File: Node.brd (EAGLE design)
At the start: 38.1 x 38.1 mm, 70 parts, among them J1 AVR_SPI_PRG_6NS, J2 M04X2, Q1 PMR280UN, Q2 PMR280UN, Q3 PMR280UN, U1 ATMEGA32U4, U2 BLUETOOTH-RN41", U4 L3GD20, U9 RCLAMP0502A, X1 USBSMD

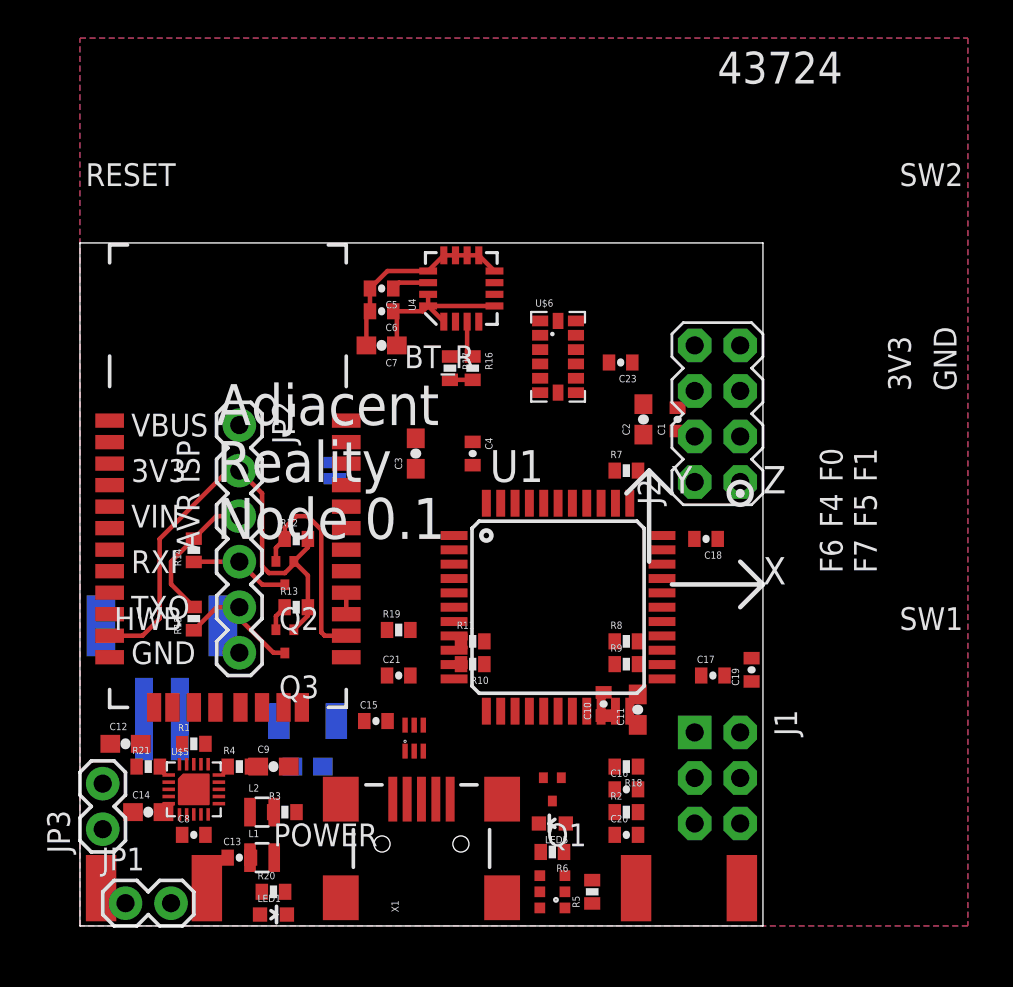
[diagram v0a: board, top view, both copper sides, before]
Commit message: mostly realistic parts placement
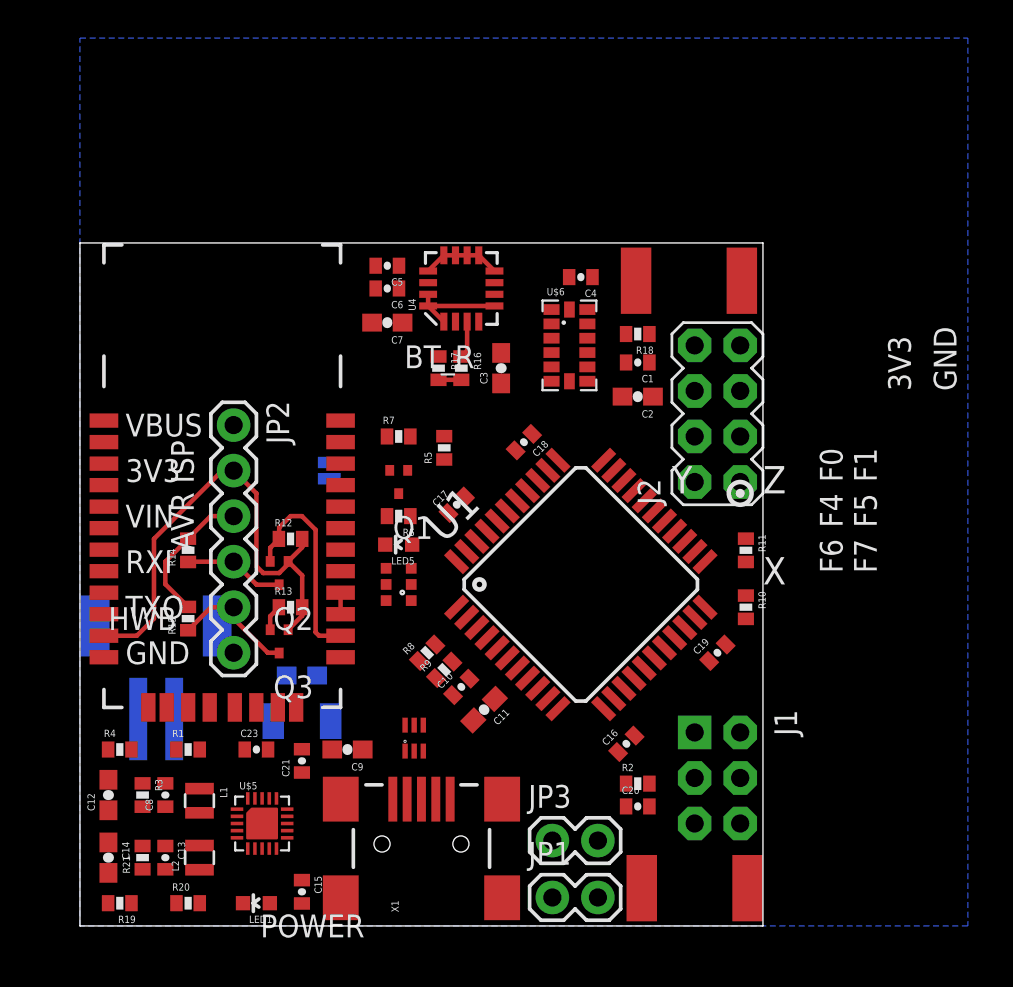
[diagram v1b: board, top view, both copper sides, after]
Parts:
- moved HWB 33.9 mm to (34.0, 36.0), turned to 180 degrees
- moved POWER 30.2 mm to (34.3, 2.11)
- moved C23 29.6 mm to (9.84, 9.84), turned to 0 degrees
- moved R5 26.1 mm to (20.3, 26.7)
- moved JP3 25.1 mm to (26.4, 4.76), turned to 0 degrees
- moved R18 24.1 mm to (31.1, 33.0)
- moved JP1 23.8 mm to (26.4, 1.59)
- moved R19 21.8 mm to (2.22, 1.27), turned to 180 degrees
- moved R6 20.6 mm to (17.8, 22.9)
- moved LED4 19.2 mm to (17.8, 19.1)
- moved Q1 19.2 mm to (17.8, 24.8)
- moved LED5 17.8 mm to (17.8, 21.3)
- moved C17 17.2 mm to (21.0, 23.5), turned to 45 degrees
- moved R11 16.1 mm to (37.1, 21.0), turned to 270 degrees
- moved R10 15.6 mm to (37.1, 17.8), turned to 270 degrees
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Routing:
- net GND: track 11.3 -> 4.42 mm
- net +3V3: track 38.8 -> 34.7 mm
- net N$7: track 2.08 -> 0.00 mm
- removed copper zone on layer 1, net GND
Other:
- board text removed: "43724"
- board text removed: "Adjacent"
- board text removed: "Node 0.1"
- board text removed: "RESET"
- board text removed: "Reality"
- board text removed: "SW1"
- board text removed: "SW2"

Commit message: pass ERC
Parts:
- BAT: value (none) -> JST
- JP1: value (none) -> POWER
- JP2: value (none) -> UART
- JP3: value (none) -> 3V3
- LED1: value (none) -> RED
- LED5: value (none) -> IR
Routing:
- net +3V3: track 34.7 -> 38.7 mm
- net SCL: track 0.00 -> 2.34 mm
- net N$7: track 0.00 -> 2.02 mm

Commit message: mostly pass DRC
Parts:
- moved C6 0.32 mm to (17.1, 35.2)
- moved C7 0.32 mm to (17.1, 33.3)
- moved U4 0.32 mm to (21.3, 35.2)
- moved C3 0.32 mm to (23.5, 30.8)
- moved R16 0.32 mm to (21.3, 30.8)
- moved R17 0.32 mm to (20.0, 30.8)
- moved C5 0.32 mm to (17.1, 36.5)
- moved POWER 0.25 mm to (34.0, 2.11)
- moved HWB 0.06 mm to (34.0, 36.0)

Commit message: more routing
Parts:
- added U$1, U$2: (no value), SparkFun-Electromechanical:STAND-OFF
- L1, L2: device adjacent-reality:VLS2016 -> adjacent-reality:VLS30
- moved JP3 25.1 mm to (1.27, 5.08)
- moved R20 21.6 mm to (26.0, 9.53)
- moved LED1 17.6 mm to (26.0, 8.26), turned to 270 degrees
- moved C22 14.0 mm to (1.27, 20.0), turned to 270 degrees
- moved R22 10.5 mm to (3.81, 20.0), turned to 270 degrees
- moved R1 10.0 mm to (11.9, 1.75), turned to 90 degrees
- moved R19 7.96 mm to (2.86, 9.21), turned to 90 degrees
- moved R4 5.51 mm to (5.87, 5.71), turned to 270 degrees
- moved C13 5.43 mm to (4.13, 9.21)
- moved C14 5.41 mm to (1.27, 9.21)
- moved L2 5.40 mm to (6.67, 9.21)
- moved C21 5.39 mm to (13.7, 3.97), turned to 0 degrees
- moved C8 5.12 mm to (4.13, 2.22)
- moved R3 5.12 mm to (2.86, 2.22)
- moved C12 5.09 mm to (1.27, 2.22), turned to 270 degrees
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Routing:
- net +3V3: track 38.7 -> 54.7 mm
- net PWR_ON1: track 0.00 -> 13.3 mm, vias 0 -> 1
- net PWR_ON2: track 0.00 -> 12.2 mm, vias 0 -> 1
- net VBUS: track 0.00 -> 12.1 mm
- net N$8: track 0.00 -> 11.1 mm, vias 0 -> 2
- net N$1: track 0.00 -> 11.1 mm
- net RESET: track 0.00 -> 9.37 mm, vias 0 -> 2
- net N$27: track 0.00 -> 9.25 mm, vias 0 -> 2
- net N$16: track 0.00 -> 8.63 mm, vias 0 -> 1
- net N$19: track 0.00 -> 8.17 mm
- net N$37: track 0.00 -> 7.89 mm
- net N$31: track 0.00 -> 7.85 mm
- net GND: track 4.42 -> 11.8 mm
- net HPWR: track 0.00 -> 6.25 mm, vias 0 -> 2
- net N$29: track 0.00 -> 5.66 mm, vias 0 -> 2
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- removed copper zone on layer 16, net GND
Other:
- board text removed: "POWER"

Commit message: route header
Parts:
- moved R5 11.6 mm to (31.9, 26.7), turned to 135 degrees
- moved C2 8.31 mm to (27.1, 36.8), turned to 0 degrees
- moved C19 7.03 mm to (36.4, 22.2), turned to 315 degrees
- moved C1 5.50 mm to (27.1, 35.2), turned to 0 degrees
- moved C4 4.67 mm to (30.6, 32.4), turned to 90 degrees
- moved R10 2.54 mm to (37.1, 15.2)
- moved R11 2.54 mm to (37.1, 18.4)
- moved LED5 1.75 mm to (17.8, 23.0)
- moved R18 1.28 mm to (32.2, 32.4), turned to 270 degrees
- moved C16 1.28 mm to (31.3, 11.1), turned to 225 degrees
- moved R6 1.27 mm to (17.8, 21.6)
- moved U$6 0.97 mm to (27.1, 31.4)
- moved J1 0.95 mm to (35.6, 10.2)
- moved J2 0.63 mm to (35.6, 27.9)
- moved C3 0.48 mm to (23.5, 30.3)
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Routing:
- net +3V3: track 54.7 -> 98.2 mm
- net RESET: track 9.37 -> 38.2 mm, vias 2 -> 4
- net HPWR: track 6.25 -> 25.5 mm
- net N$34: track 0.00 -> 18.1 mm, vias 0 -> 1
- net N$8: track 11.1 -> 27.9 mm
- net N$35: track 0.00 -> 16.7 mm, vias 0 -> 1
- net N$32: track 0.00 -> 14.6 mm, vias 0 -> 1
- net MOSI: track 0.00 -> 14.6 mm, vias 0 -> 1
- net HWB: track 0.00 -> 14.3 mm
- net N$33: track 0.00 -> 13.2 mm, vias 0 -> 1
- net N$28: track 0.00 -> 12.6 mm, vias 0 -> 1
- net SCK: track 0.00 -> 12.0 mm, vias 0 -> 1
- net N$30: track 0.00 -> 10.6 mm, vias 0 -> 1
- net VBUS: track 12.1 -> 21.3 mm
- net MISO: track 0.00 -> 8.17 mm, vias 0 -> 1
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
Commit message: mostly complete routing
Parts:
- moved R5 17.1 mm to (18.4, 16.2), turned to 225 degrees
- moved LED1 1.59 mm to (27.3, 7.30)
- moved R20 1.50 mm to (27.3, 8.73)
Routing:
- net RBT: track 0.00 -> 42.5 mm, vias 0 -> 2
- net SCL: track 9.78 -> 36.0 mm, vias 2 -> 4
- net SDA: track 6.73 -> 31.6 mm, vias 0 -> 2
- net TX: track 1.48 -> 23.6 mm, vias 0 -> 2
- net PWR_ON1: track 13.3 -> 34.7 mm
- net RX: track 11.9 -> 33.2 mm, vias 0 -> 2
- net PWR_ON2: track 12.2 -> 31.4 mm, vias 1 -> 2
- net N$1: track 11.1 -> 29.6 mm, vias 0 -> 2
- net PCINT4: track 0.00 -> 17.1 mm, vias 0 -> 2
- net N$17: track 0.00 -> 16.8 mm, vias 0 -> 2
- net N$16: track 8.63 -> 25.1 mm, vias 1 -> 4
- net +3V3: track 98.2 -> 114.1 mm
- net N$22: track 1.48 -> 16.5 mm, vias 0 -> 2
- net N$12: track 0.00 -> 14.6 mm, vias 0 -> 2
- net N$18: track 4.20 -> 16.6 mm, vias 0 -> 2
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
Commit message: fix a bunch of tiny air wires
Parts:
- moved BAT 3.52 mm to (4.47, 9.65), turned to 180 degrees
- moved SJ1 3.49 mm to (10.4, 25.4)
- moved C22 3.20 mm to (4.47, 20.2), turned to 180 degrees
- moved R22 2.62 mm to (4.47, 17.5), turned to 180 degrees
- moved R10 0.32 mm to (36.8, 15.2)
- moved R11 0.32 mm to (36.8, 18.4)
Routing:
- net +3V3: track 114.1 -> 161.3 mm, vias 0 -> 4
- net VBUS: track 21.3 -> 43.4 mm, vias 0 -> 4
- net N$1: track 29.6 -> 48.3 mm, vias 2 -> 4
- net PWR_ON1: track 34.7 -> 52.0 mm, vias 1 -> 2
- net N$29: track 5.66 -> 20.8 mm, vias 2 -> 3
- net SBT: track 0.00 -> 8.55 mm, vias 0 -> 2
- net HWB: track 7.11 -> 15.1 mm, vias 0 -> 2
- net N$14: track 0.00 -> 5.50 mm, vias 0 -> 1
- net TX: track 23.6 -> 28.2 mm
- net GND: track 11.8 -> 16.1 mm, vias 0 -> 31
- net N$27: track 9.25 -> 12.6 mm
- net N$36: track 0.00 -> 3.01 mm
- net HPWR: track 25.5 -> 23.7 mm
- net VDIV: track 6.49 -> 7.95 mm
- net SCK: track 12.0 -> 12.7 mm
- added copper zone on layer 1, net GND
- added copper zone on layer 16, net GND

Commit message: one wire left
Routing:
- net +3V3: track 161.3 -> 182.2 mm, vias 4 -> 7
- net N$30: track 10.6 -> 11.7 mm
- net N$28: track 12.6 -> 13.5 mm
- net N$12: track 14.6 -> 15.3 mm
- net GND: vias 31 -> 29
